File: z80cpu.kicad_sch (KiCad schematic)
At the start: 11 parts

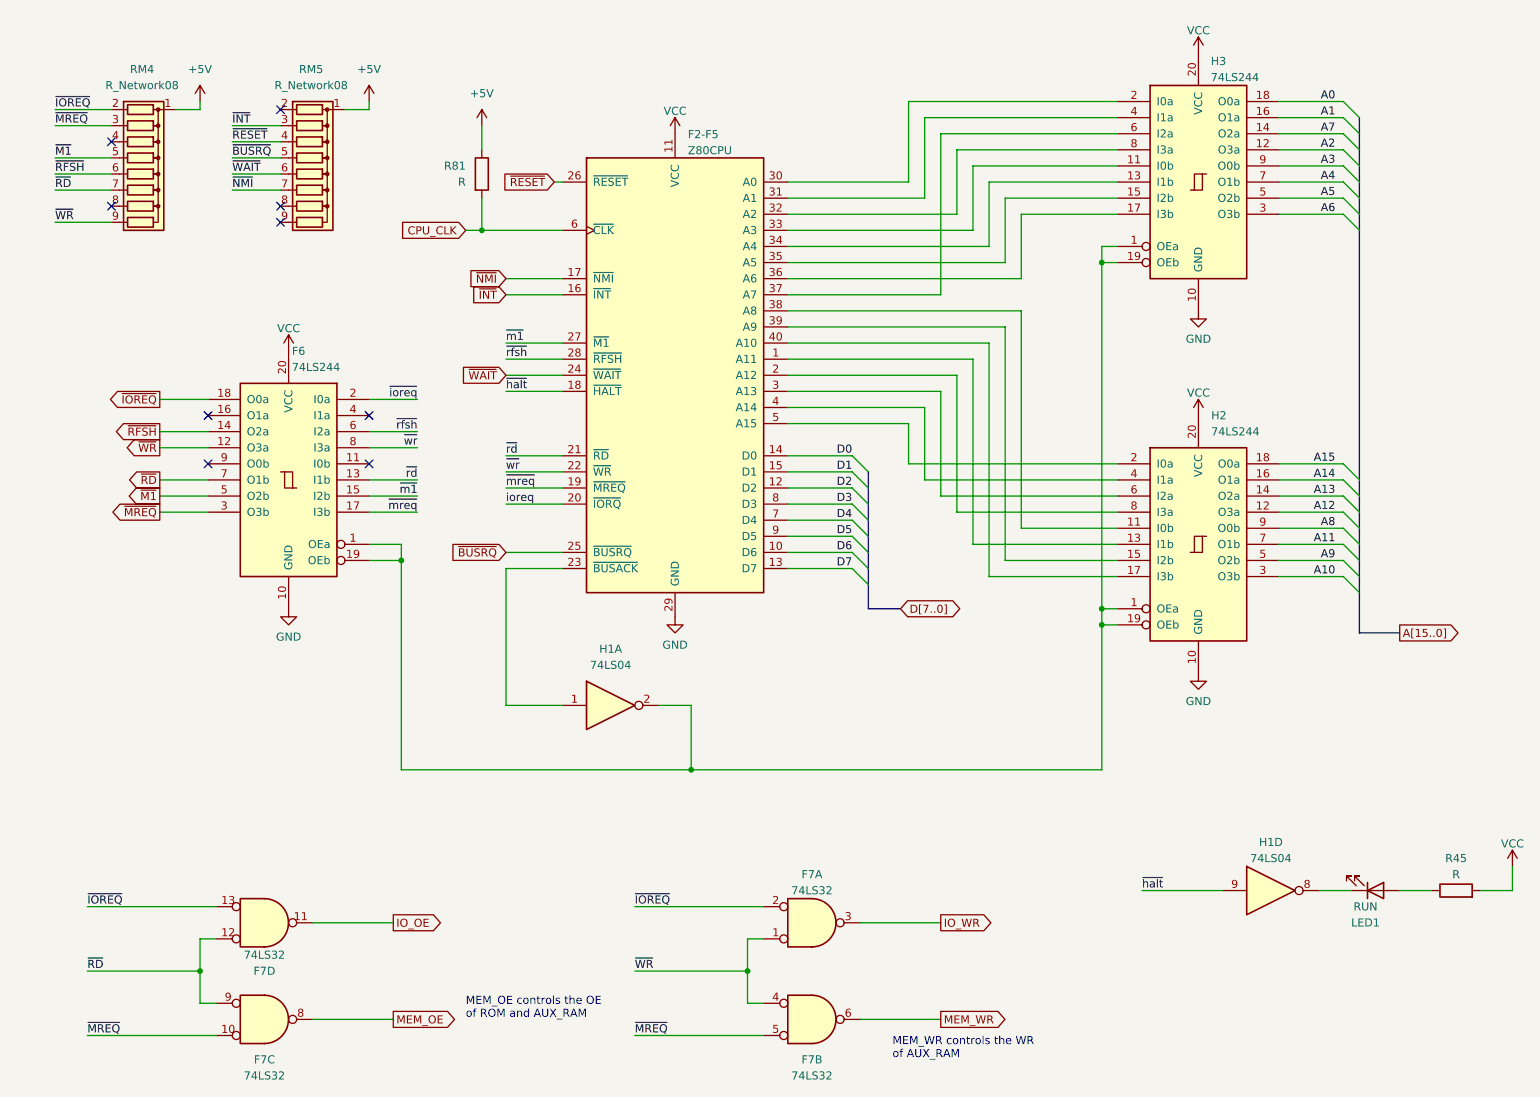
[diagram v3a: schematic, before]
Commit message: Components renaming according to the Uxy convention.
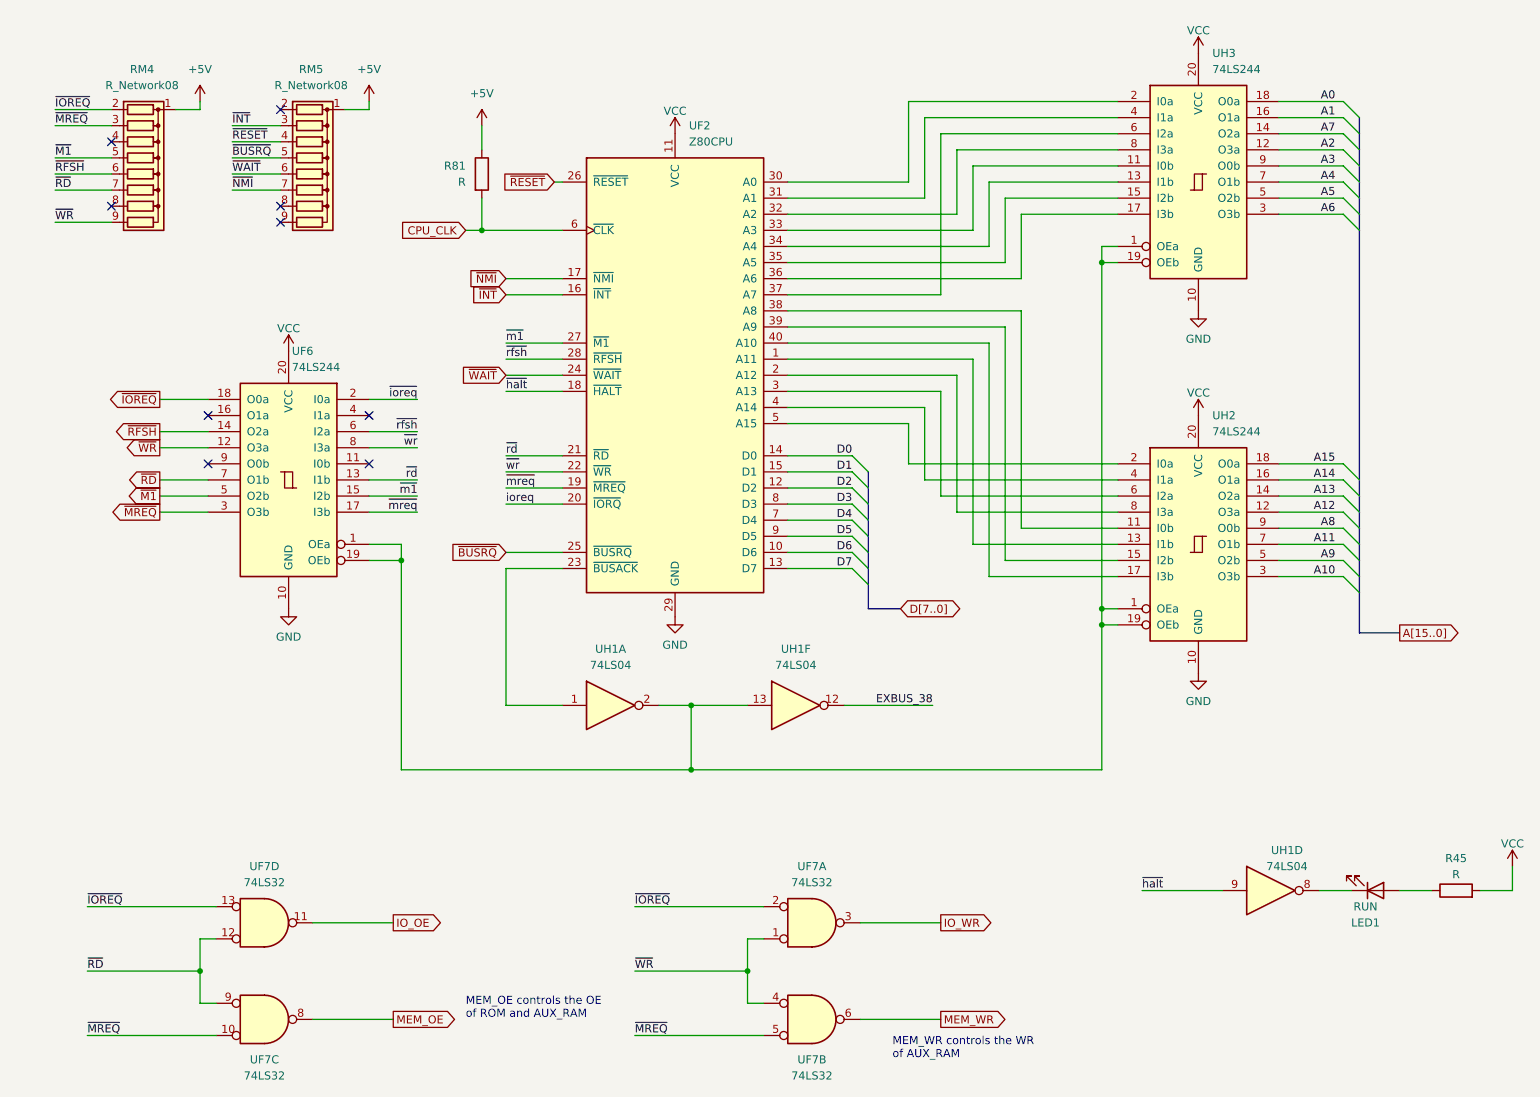
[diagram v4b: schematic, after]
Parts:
- added unit 6 of UH1
- renumbered F2-F5 to UF2, F6 to UF6, F7 to UF7, H1 to UH1, H2 to UH2, H3 to UH3
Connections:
- net at UF6.1 (OEa), UF6.19 (OEb), UH1.2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: now also UH1.13
- new net EXBUS_38: UH1.12
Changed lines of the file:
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@@
   (junction (at 118.11 134.62) (diameter 0) (color 0 0 0 0)
+  )
+  (junction (at 118.11 124.46) (diameter 0) (color 0 0 0 0)
   )
   (junction (at 182.88 111.76) (diameter 0) (color 0 0 0 0)
@@
     (stroke (width 0) (type default))
   )
+  (wire (pts (xy 142.24 124.46) (xy 156.21 124.46))
+    (stroke (width 0) (type default))
+  )
   (wire (pts (xy 242.57 153.67) (xy 247.65 153.67))
     (stroke (width 0) (type default))
   )
+  (wire (pts (xy 118.11 124.46) (xy 127 124.46))
+    (stroke (width 0) (type default))
+  )
   (bus (pts (xy 146.05 102.87) (xy 146.05 105.41))
     (stroke (width 0) (type default))
@@
   (label "~{rfsh}" (at 88.9 69.85 0) (fields_autoplaced)
     (effects (font (size 1.27 1.27)) (justify left bottom))
+  )
+  (label "EXBUS_38" (at 156.21 124.46 180) (fields_autoplaced)
+    (effects (font (size 1.27 1.27)) (justify right bottom))
   )
   (label "~{WR}" (at 109.22 166.37 0) (fields_autoplaced)
@@
   )
   (symbol (lib_id "74xx:74LS32") (at 137.16 173.99 0) (unit 2) (convert 2)
-    (in_bom yes) (on_board yes) (dnp no) (fields_autoplaced)
-    (property "Reference" "F7" (at 137.16 180.34 0)
+    (in_bom yes) (on_board yes) (dnp no)
+    (property "Reference" "UF7" (at 137.16 180.34 0)
       (effects (font (size 1.27 1.27)))
     )
@@
       (project "ceda"
         (path "/12a6dbe3-008d-4c5b-88f6-9f1c816060be/1847fdc4-53d8-4940-8c5f-7a326599bae2"
-          (reference "F7") (unit 2)
+          (reference "UF7") (unit 2)
         )
       )
@@
   )
   (symbol (lib_id "74xx:74LS32") (at 50.8 173.99 0) (unit 3) (convert 2)
-    (in_bom yes) (on_board yes) (dnp no) (fields_autoplaced)
-    (property "Reference" "F7" (at 50.8 180.34 0)
+    (in_bom yes) (on_board yes) (dnp no)
+    (property "Reference" "UF7" (at 50.8 180.34 0)
       (effects (font (size 1.27 1.27)))
     )
@@
       (project "ceda"
         (path "/12a6dbe3-008d-4c5b-88f6-9f1c816060be/1847fdc4-53d8-4940-8c5f-7a326599bae2"
-          (reference "F7") (unit 3)
+          (reference "UF7") (unit 3)
         )
       )
@@
   (symbol (lib_id "74xx:74LS244") (at 198.12 41.91 0) (unit 1)
     (in_bom yes) (on_board yes) (dnp no) (fields_autoplaced)
-    (property "Reference" "H3" (at 200.0759 22.86 0)
+    (property "Reference" "UH3" (at 200.3141 21.59 0)
       (effects (font (size 1.27 1.27)) (justify left))
     )
-    (property "Value" "74LS244" (at 200.0759 25.4 0)
+    (property "Value" "74LS244" (at 200.3141 24.13 0)
       (effects (font (size 1.27 1.27)) (justify left))
     )
@@
       (project "ceda"
         (path "/12a6dbe3-008d-4c5b-88f6-9f1c816060be/1847fdc4-53d8-4940-8c5f-7a326599bae2"
-          (reference "H3") (unit 1)
+          (reference "UH3") (unit 1)
         )
       )
@@
   (symbol (lib_id "CPU:Z80CPU") (at 115.57 72.39 0) (unit 1)
     (in_bom yes) (on_board yes) (dnp no) (fields_autoplaced)
-    (property "Reference" "F2-F5" (at 117.5894 34.4002 0)
+    (property "Reference" "UF2" (at 117.7641 33.02 0)
       (effects (font (size 1.27 1.27)) (justify left))
     )
-    (property "Value" "Z80CPU" (at 117.5894 36.9371 0)
+    (property "Value" "Z80CPU" (at 117.7641 35.56 0)
       (effects (font (size 1.27 1.27)) (justify left))
     )
@@
       (project "ceda"
         (path "/12a6dbe3-008d-4c5b-88f6-9f1c816060be/1847fdc4-53d8-4940-8c5f-7a326599bae2"
-          (reference "F2-F5") (unit 1)
+          (reference "UF2") (unit 1)
         )
       )
@@
   )
   (symbol (lib_id "74xx:74LS04") (at 209.55 153.67 0) (unit 4)
-    (in_bom yes) (on_board yes) (dnp no) (fields_autoplaced)
-    (property "Reference" "H1" (at 209.55 146.05 0)
-      (effects (font (size 1.27 1.27)))
-    )
-    (property "Value" "74LS04" (at 209.55 148.59 0)
+    (in_bom yes) (on_board yes) (dnp no)
+    (property "Reference" "UH1" (at 212.09 147.32 0)
+      (effects (font (size 1.27 1.27)))
+    )
+    (property "Value" "74LS04" (at 212.09 149.86 0)
       (effects (font (size 1.27 1.27)))
     )
@@
       (project "ceda"
         (path "/12a6dbe3-008d-4c5b-88f6-9f1c816060be/1847fdc4-53d8-4940-8c5f-7a326599bae2"
-          (reference "H1") (unit 4)
+          (reference "UH1") (unit 4)
         )
       )
@@
   (symbol (lib_id "74xx:74LS244") (at 198.12 99.06 0) (unit 1)
     (in_bom yes) (on_board yes) (dnp no) (fields_autoplaced)
-    (property "Reference" "H2" (at 200.1394 78.74 0)
+    (property "Reference" "UH2" (at 200.3141 78.74 0)
       (effects (font (size 1.27 1.27)) (justify left))
     )
-    (property "Value" "74LS244" (at 200.1394 81.28 0)
+    (property "Value" "74LS244" (at 200.3141 81.28 0)
       (effects (font (size 1.27 1.27)) (justify left))
     )
@@
       (project "ceda"
         (path "/12a6dbe3-008d-4c5b-88f6-9f1c816060be/1847fdc4-53d8-4940-8c5f-7a326599bae2"
-          (reference "H2") (unit 1)
+          (reference "UH2") (unit 1)
         )
       )
@@
   (symbol (lib_id "74xx:74LS244") (at 54.61 88.9 0) (mirror y) (unit 1)
     (in_bom yes) (on_board yes) (dnp no)
-    (property "Reference" "F6" (at 55.1306 68.58 0)
+    (property "Reference" "UF6" (at 55.1306 68.58 0)
       (effects (font (size 1.27 1.27)) (justify right))
     )
@@
       (project "ceda"
         (path "/12a6dbe3-008d-4c5b-88f6-9f1c816060be/1847fdc4-53d8-4940-8c5f-7a326599bae2"
-          (reference "F6") (unit 1)
-        )
-      )
-    )
-  )
-  (symbol (lib_id "74xx:74LS04") (at 105.41 124.46 0) (unit 1)
-    (in_bom yes) (on_board yes) (dnp no) (fields_autoplaced)
-    (property "Reference" "H1" (at 105.41 115.57 0)
-      (effects (font (size 1.27 1.27)))
-    )
-    (property "Value" "74LS04" (at 105.41 118.11 0)
-      (effects (font (size 1.27 1.27)))
-    )
-    (property "Footprint" "" (at 105.41 124.46 0)
-      (effects (font (size 1.27 1.27)) hide)
-    )
-    (property "Datasheet" "http://www.ti.com/lit/gpn/sn74LS04" (at 105.41 124.46 0)
+          (reference "UF6") (unit 1)
+        )
+      )
+    )
+  )
+  (symbol (lib_id "74xx:74LS04") (at 134.62 124.46 0) (unit 6)
+    (in_bom yes) (on_board yes) (dnp no) (fields_autoplaced)
+    (property "Reference" "UH1" (at 134.62 115.57 0)
+      (effects (font (size 1.27 1.27)))
+    )
+    (property "Value" "74LS04" (at 134.62 118.11 0)
+      (effects (font (size 1.27 1.27)))
+    )
+    (property "Footprint" "" (at 134.62 124.46 0)
+      (effects (font (size 1.27 1.27)) hide)
+    )
+    (property "Datasheet" "http://www.ti.com/lit/gpn/sn74LS04" (at 134.62 124.46 0)
       (effects (font (size 1.27 1.27)) hide)
     )
@@
       (project "ceda"
         (path "/12a6dbe3-008d-4c5b-88f6-9f1c816060be/1847fdc4-53d8-4940-8c5f-7a326599bae2"
-          (reference "H1") (unit 1)
+          (reference "UH1") (unit 6)
+        )
+      )
+    )
+  )
+  (symbol (lib_id "74xx:74LS04") (at 105.41 124.46 0) (unit 1)
+    (in_bom yes) (on_board yes) (dnp no) (fields_autoplaced)
+    (property "Reference" "UH1" (at 105.41 115.57 0)
+      (effects (font (size 1.27 1.27)))
+    )
+    (property "Value" "74LS04" (at 105.41 118.11 0)
+      (effects (font (size 1.27 1.27)))
+    )
+    (property "Footprint" "" (at 105.41 124.46 0)
+      (effects (font (size 1.27 1.27)) hide)
+    )
+    (property "Datasheet" "http://www.ti.com/lit/gpn/sn74LS04" (at 105.41 124.46 0)
+      (effects (font (size 1.27 1.27)) hide)
+    )
+    (pin "1")
+    (pin "2")
+    (pin "3")
+    (pin "4")
+    (pin "5")
+    (pin "6")
+    (pin "8")
+    (pin "9")
+    (pin "10")
+    (pin "11")
+    (pin "12")
+    (pin "13")
+    (pin "14")
+    (pin "7")
+    (instances
+      (project "ceda"
+        (path "/12a6dbe3-008d-4c5b-88f6-9f1c816060be/1847fdc4-53d8-4940-8c5f-7a326599bae2"
+          (reference "UH1") (unit 1)
         )
       )
@@
   )
   (symbol (lib_id "74xx:74LS32") (at 50.8 158.75 0) (mirror x) (unit 4) (convert 2)
-    (in_bom yes) (on_board yes) (dnp no)
-    (property "Reference" "F7" (at 50.8 166.37 0)
-      (effects (font (size 1.27 1.27)))
-    )
-    (property "Value" "74LS32" (at 50.8 163.83 0)
+    (in_bom yes) (on_board yes) (dnp no) (fields_autoplaced)
+    (property "Reference" "UF7" (at 50.7917 149.86 0)
+      (effects (font (size 1.27 1.27)))
+    )
+    (property "Value" "74LS32" (at 50.7917 152.4 0)
       (effects (font (size 1.27 1.27)))
     )
@@
       (project "ceda"
         (path "/12a6dbe3-008d-4c5b-88f6-9f1c816060be/1847fdc4-53d8-4940-8c5f-7a326599bae2"
-          (reference "F7") (unit 4)
+          (reference "UF7") (unit 4)
         )
       )
@@
   (symbol (lib_id "74xx:74LS32") (at 137.16 158.75 0) (mirror x) (unit 1) (convert 2)
     (in_bom yes) (on_board yes) (dnp no) (fields_autoplaced)
-    (property "Reference" "F7" (at 137.16 151.13 0)
-      (effects (font (size 1.27 1.27)))
-    )
-    (property "Value" "74LS32" (at 137.16 153.67 0)
+    (property "Reference" "UF7" (at 137.1517 149.86 0)
+      (effects (font (size 1.27 1.27)))
+    )
+    (property "Value" "74LS32" (at 137.1517 152.4 0)
       (effects (font (size 1.27 1.27)))
     )
@@
       (project "ceda"
         (path "/12a6dbe3-008d-4c5b-88f6-9f1c816060be/1847fdc4-53d8-4940-8c5f-7a326599bae2"
-          (reference "F7") (unit 1)
-        )
-      )
+          (reference "UF7") (unit 1)
+        )
+      )
